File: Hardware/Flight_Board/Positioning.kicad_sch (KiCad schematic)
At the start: 0 parts

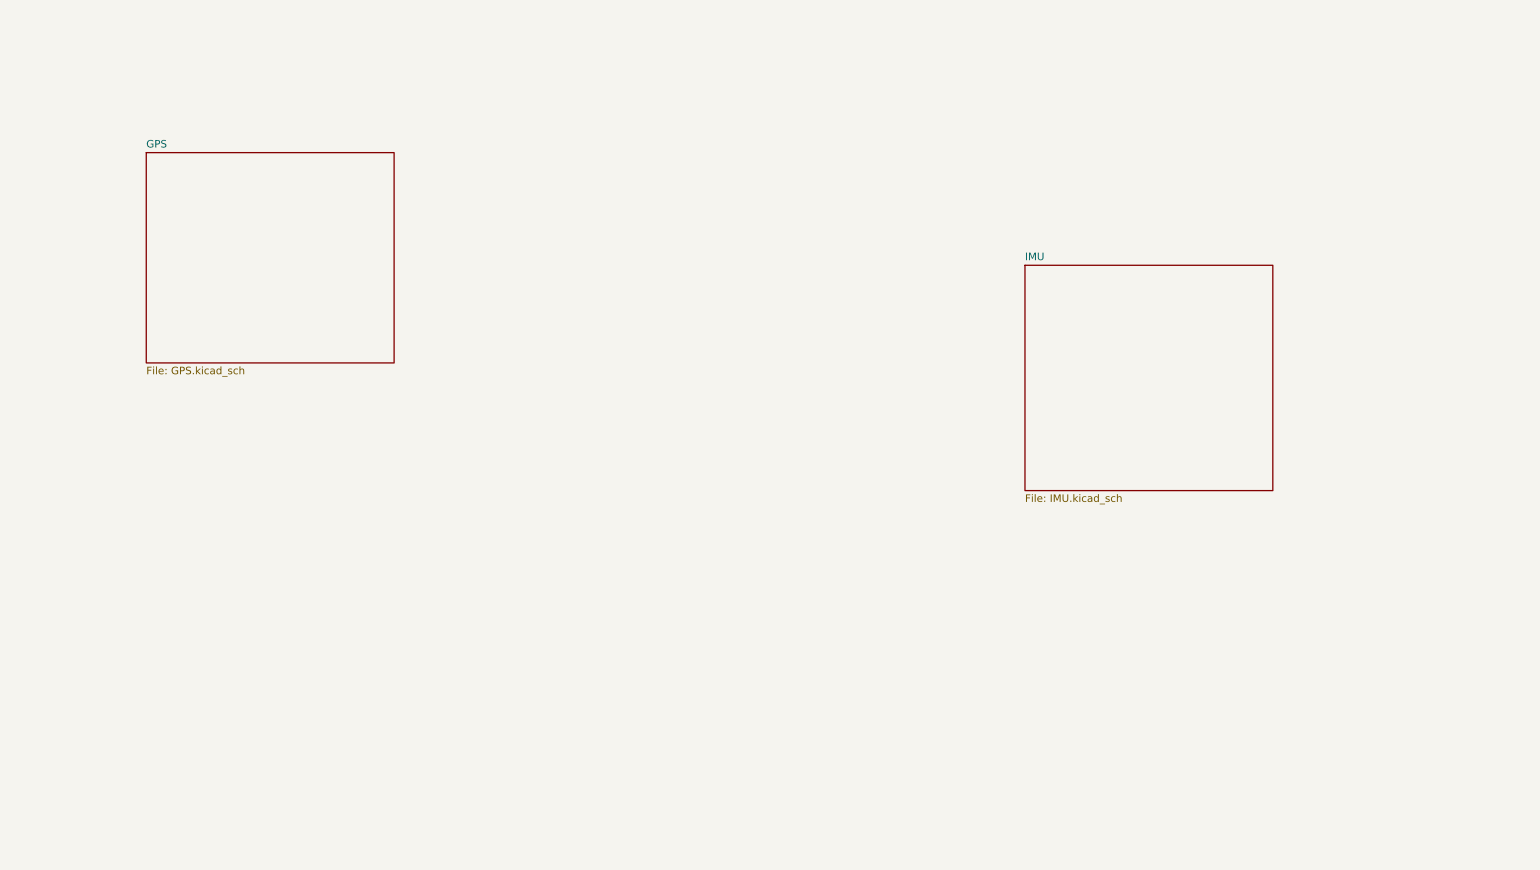
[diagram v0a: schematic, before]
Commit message: Harware GPS, Radio, Power, IMU, Barrometer Prototypes
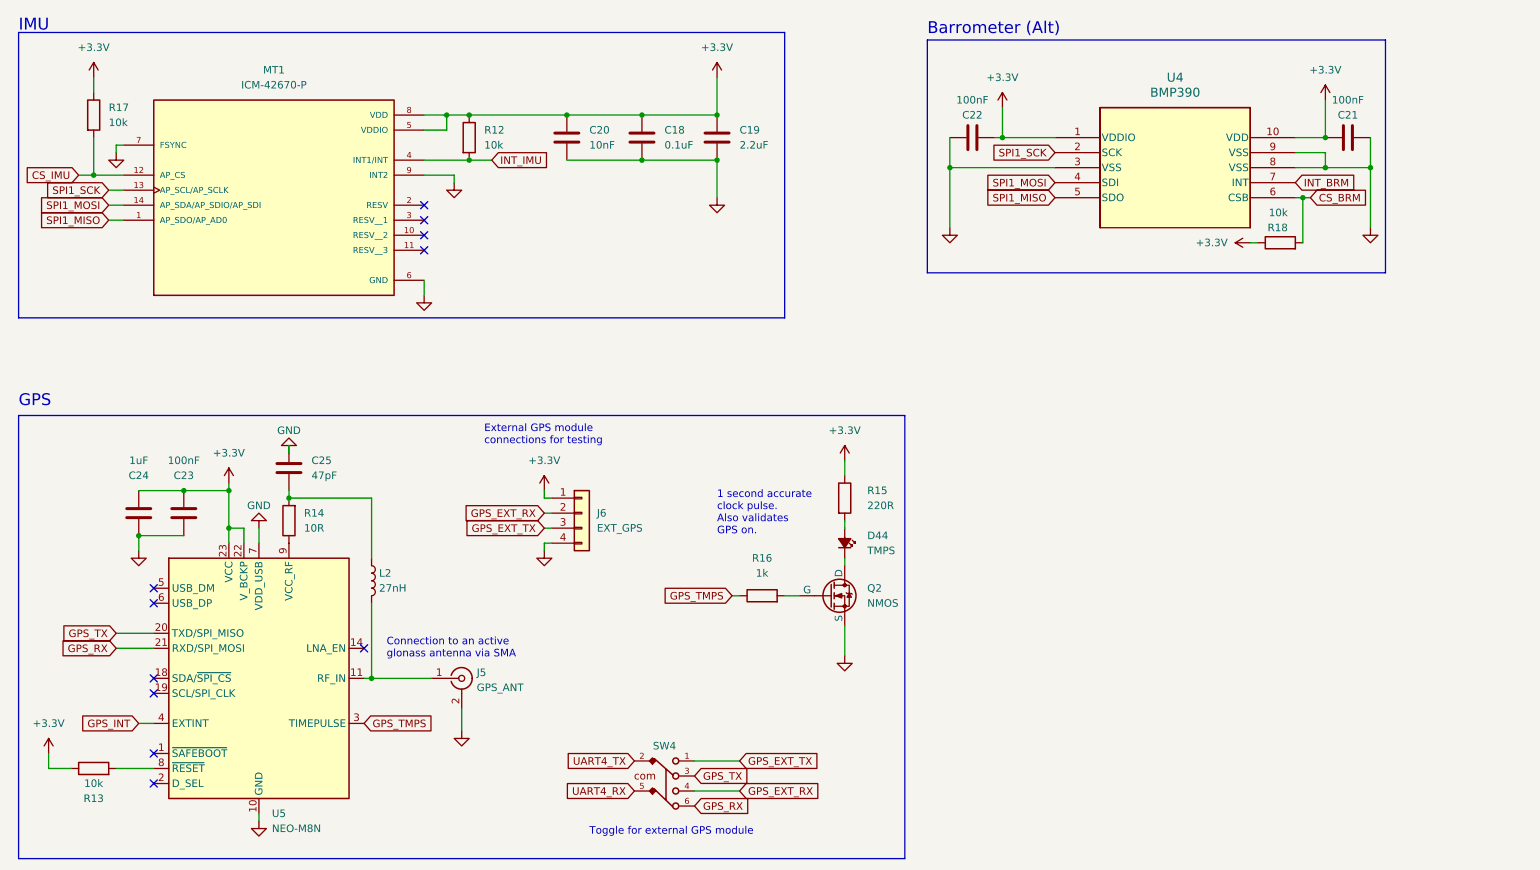
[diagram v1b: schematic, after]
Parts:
- added C18: 0.1uF, symbol Device:C
- added C19: 2.2uF, symbol Device:C
- added C20: 10nF, symbol Device:C
- added C21, C22, C23: 100nF, symbol Device:C
- added C24: 1uF, symbol Device:C
- added C25: 47pF, symbol Device:C
- added D44: TMPS, LED_SMD:LED_0603_1608Metric, symbol Device:LED_Small_Filled
- added J5: GPS_ANT, symbol Connector:Conn_Coaxial
- added J6: EXT_GPS, symbol Connector_Generic:Conn_01x04
- added L2: 27nH, symbol Device:L
- added MT1: ICM-42670-P, ICM-42670-P:XDCR_ICM-42670-P, symbol Sensor_Motion:ICM-42670-P
- added Q2: NMOS, symbol Simulation_SPICE:NMOS
- added R12, R13, R17, R18: 10k, symbol Device:R
- added R14: 10R, symbol Device:R
- added R15: 220R, symbol Device:R
- added R16: 1k, symbol Device:R
- added SW4: DPDT_Slide_SMD, 452403012014:452403012014, symbol Switch:DPDT_Slide_SMD
- added U4: BMP390, 10LGA_2X2X0p75_BOS, symbol Sensor_Pressure:BMP390
- added U5: NEO-M8N, RF_GPS:ublox_NEO, symbol RF_GPS:NEO-M8N
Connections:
- new net: D44.1 (K), Q2.1 (D)
- new net: Q2.2 (G), R16.2
- new net: D44.2 (A), R15.2
- new net: R14.1, U5.9 (VCC_RF)
- new net: C25.2, L2.1, R14.2
- new net: J5.1 (In), L2.2, U5.11 (RF_IN)
- new net: R13.2, U5.8 (~{RESET})
- new net +3.3V: C18.1, C19.1, C20.1, C21.1, C22.1, C23.1, C24.1, J6.1 (Pin_1), MT1.5 (VDDIO), MT1.8 (VDD), R12.1, R13.1, R15.1, R17.1, R18.1, U4.1 (VDDIO), U4.10 (VDD), U5.22 (V_BCKP), U5.23 (VCC)
- new net CS_BRM: R18.2, U4.6 (CSB)
- new net CS_IMU: MT1.12 (AP_CS), R17.2
- new net GND: C18.2, C19.2, C20.2, C21.2, C22.2, C23.2, C24.2, C25.1, J5.2 (Ext), J6.4 (Pin_4), MT1.6 (GND), MT1.7 (FSYNC), MT1.9 (INT2), Q2.3 (S), U4.3 (VSS), U4.8 (VSS), U4.9 (VSS), U5.10 (GND), U5.12 (GND), U5.13 (GND), U5.24 (GND), U5.7 (VDD_USB)
- new net GPS_EXT_RX: J6.2 (Pin_2), SW4.4
- new net GPS_EXT_TX: J6.3 (Pin_3), SW4.1
- new net GPS_INT: U5.4 (EXTINT)
- new net GPS_RX: SW4.6, U5.21 (RXD/SPI_MOSI)
- new net GPS_TMPS: R16.1, U5.3 (TIMEPULSE)
- new net GPS_TX: SW4.3, U5.20 (TXD/SPI_MISO)
- new net INT_BRM: U4.7 (INT)
- new net INT_IMU: MT1.4 (INT1/INT), R12.2
- new net SPI1_MISO: MT1.1 (AP_SDO/AP_AD0), U4.5 (SDO)
- new net SPI1_MOSI: MT1.14 (AP_SDA/AP_SDIO/AP_SDI), U4.4 (SDI)
- new net SPI1_SCK: MT1.13 (AP_SCL/AP_SCLK), U4.2 (SCK)
- new net UART4_RX: SW4.5
- new net UART4_TX: SW4.2
- no-connect marks 0 -> 11
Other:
- removed sheet GPS
- removed sheet IMU
- note added: "1 second accurate clock pulse. Also validates GPS on."
- note added: "Barrometer (Alt)"
- note added: "Connection to an active glonass antenna via SMA"
- note added: "External GPS module connections for testing"
- note added: "GPS"
- note added: "IMU"
- note added: "Toggle for external GPS module"

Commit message: ESC Rough Draft
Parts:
- added C35, C36: 100nF, symbol Device:C
- added R21, R22: 100R, symbol Device:R
- added R23, R24: 1.2k, symbol Device:R
- added U8: TLV493D, Package_TO_SOT_SMD:SOT-23-6, symbol Sensor_Magnetic:TLV493D
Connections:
- net +3.3V: now also C35.2, R23.1, R24.1, U8.4 (VDD)
- net GND: now also C35.1, C36.1, U8.2 (GND), U8.3 (GND), U8.5 (GND)
- new net: R21.2, U8.1 (SCL/INT)
- new net: R22.2, U8.6 (SDA/ADDR)
- new net SCL: R21.1, R23.2
- new net SDA: C36.2, R22.1, R24.2
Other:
- note added: "Rotational Sensor"
